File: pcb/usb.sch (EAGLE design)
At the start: 25 parts, among them J1 JSTPH, Q1 ZXMP6A13FTA, Q2 mmbt2222, Q3 mmbt2222, U1 MIC5225-3.3v, U2 CH340C, U3 MCP73831T-2ACI/OT

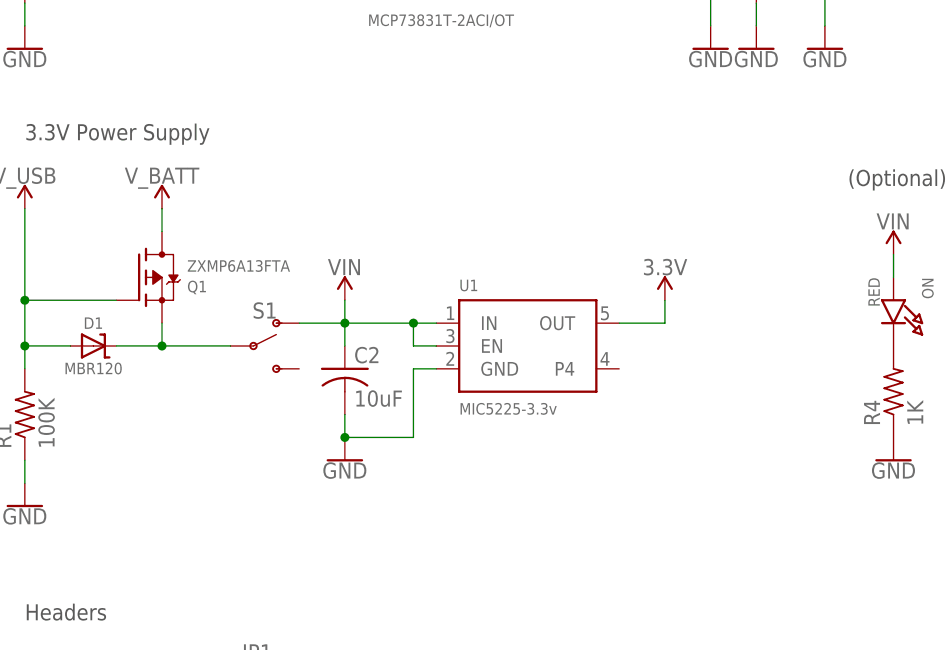
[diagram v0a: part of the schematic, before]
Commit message: Add jumper to bypass switch on USB board
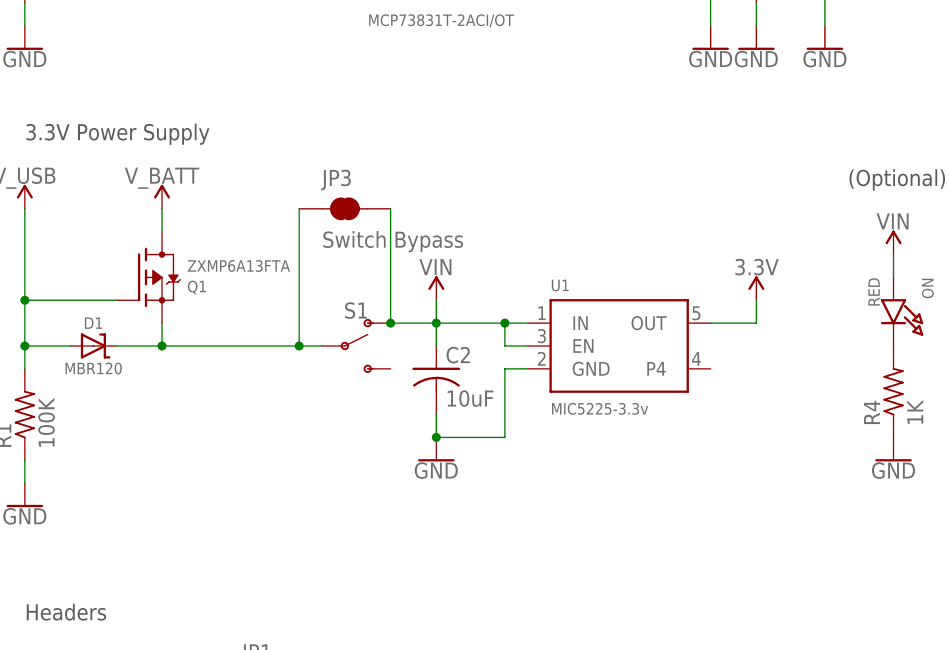
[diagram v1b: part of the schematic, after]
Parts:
- added JP3: Switch Bypass, SparkFun-Jumpers:JUMPER-SMT_2_NC_TRACE_NO-SILK
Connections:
- net N$7: now also JP3.1
- net VIN: now also JP3.2
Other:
- moved on the sheet: C2, S1, U1
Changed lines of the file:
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@@
 <attribute name="MPN" value="LMK212BJ106KG-T"/>
 </part>
+<part name="JP3" library="SparkFun-Jumpers" library_urn="urn:adsk.eagle:library:528" deviceset="JUMPER-SMT_2_NC_TRACE" device="_NO-SILK" package3d_urn="urn:adsk.eagle:package:39286/1" value="Switch Bypass"/>
 </parts>
 <sheets>
@@
 </plain>
 <instances>
-<instance part="U1" gate="G$1" x="73.66" y="68.58" smashed="yes">
-<attribute name="NAME" x="66.04" y="74.676" size="1.27" layer="95"/>
-<attribute name="VALUE" x="66.04" y="60.96" size="1.27" layer="95"/>
-<attribute name="MPN" x="73.66" y="68.58" size="1.778" layer="96" display="off"/>
+<instance part="U1" gate="G$1" x="83.82" y="68.58" smashed="yes">
+<attribute name="NAME" x="76.2" y="74.676" size="1.27" layer="95"/>
+<attribute name="VALUE" x="76.2" y="60.96" size="1.27" layer="95"/>
+<attribute name="MPN" x="83.82" y="68.58" size="1.778" layer="96" display="off"/>
 </instance>
 <instance part="U3" gate="G$1" x="66.04" y="116.84" smashed="yes">
@@
 <attribute name="MPN" x="33.02" y="76.2" size="1.778" layer="96" rot="MR180" display="off"/>
 </instance>
-<instance part="S1" gate="1" x="43.18" y="68.58" smashed="yes">
-<attribute name="NAME" x="44.45" y="71.628" size="1.778" layer="95" font="vector" align="bottom-center"/>
-<attribute name="VALUE" x="44.196" y="65.278" size="1.778" layer="96" font="vector" align="top-center"/>
-<attribute name="MPN" x="43.18" y="68.58" size="1.778" layer="96" display="off"/>
+<instance part="S1" gate="1" x="53.34" y="68.58" smashed="yes">
+<attribute name="NAME" x="54.61" y="71.628" size="1.778" layer="95" font="vector" align="bottom-center"/>
+<attribute name="VALUE" x="54.356" y="65.278" size="1.778" layer="96" font="vector" align="top-center"/>
+<attribute name="MPN" x="53.34" y="68.58" size="1.778" layer="96" display="off"/>
 </instance>
 <instance part="U2" gate="U1" x="187.96" y="119.38" smashed="yes">
@@
 <attribute name="VALUE" x="17.78" y="129.794" size="1.778" layer="96" align="bottom-center"/>
 </instance>
-<instance part="SUPPLY5" gate="G$1" x="88.9" y="73.66" smashed="yes">
-<attribute name="VALUE" x="88.9" y="76.454" size="1.778" layer="96" font="vector" align="bottom-center"/>
-</instance>
-<instance part="SUPPLY4" gate="G$1" x="53.34" y="73.66" smashed="yes">
-<attribute name="VALUE" x="53.34" y="76.454" size="1.778" layer="96" align="bottom-center"/>
+<instance part="SUPPLY5" gate="G$1" x="99.06" y="73.66" smashed="yes">
+<attribute name="VALUE" x="99.06" y="76.454" size="1.778" layer="96" font="vector" align="bottom-center"/>
+</instance>
+<instance part="SUPPLY4" gate="G$1" x="63.5" y="73.66" smashed="yes">
+<attribute name="VALUE" x="63.5" y="76.454" size="1.778" layer="96" align="bottom-center"/>
 </instance>
 <instance part="SUPPLY7" gate="G$1" x="114.3" y="78.74" smashed="yes">
@@
 <attribute name="VALUE" x="17.78" y="50.546" size="1.778" layer="96" align="top-center"/>
 </instance>
-<instance part="GND3" gate="1" x="53.34" y="55.88" smashed="yes">
-<attribute name="VALUE" x="53.34" y="55.626" size="1.778" layer="96" align="top-center"/>
+<instance part="GND3" gate="1" x="63.5" y="55.88" smashed="yes">
+<attribute name="VALUE" x="63.5" y="55.626" size="1.778" layer="96" align="top-center"/>
 </instance>
 <instance part="GND7" gate="1" x="114.3" y="55.88" smashed="yes">
@@
 <attribute name="VALUE" x="172.72" y="106.426" size="1.778" layer="96" align="top-center"/>
 </instance>
-<instance part="C2" gate="G$1" x="53.34" y="66.04" smashed="yes">
-<attribute name="NAME" x="54.356" y="66.675" size="1.778" layer="95"/>
-<attribute name="VALUE" x="54.356" y="61.849" size="1.778" layer="96"/>
-<attribute name="MPN" x="53.34" y="66.04" size="1.778" layer="96" display="off"/>
+<instance part="C2" gate="G$1" x="63.5" y="66.04" smashed="yes">
+<attribute name="NAME" x="64.516" y="66.675" size="1.778" layer="95"/>
+<attribute name="VALUE" x="64.516" y="61.849" size="1.778" layer="96"/>
+<attribute name="MPN" x="63.5" y="66.04" size="1.778" layer="96" display="off"/>
+</instance>
+<instance part="JP3" gate="G$1" x="53.34" y="83.82" smashed="yes">
+<attribute name="NAME" x="50.8" y="86.36" size="1.778" layer="95" font="vector"/>
+<attribute name="VALUE" x="50.8" y="81.28" size="1.778" layer="96" font="vector" align="top-left"/>
 </instance>
 </instances>
@@
 </segment>
 <segment>
-<wire x1="63.5" y1="66.04" x2="60.96" y2="66.04" width="0.1524" layer="91"/>
-<wire x1="60.96" y1="66.04" x2="60.96" y2="58.42" width="0.1524" layer="91"/>
-<wire x1="53.34" y1="60.96" x2="53.34" y2="58.42" width="0.1524" layer="91"/>
-<wire x1="53.34" y1="58.42" x2="60.96" y2="58.42" width="0.1524" layer="91"/>
+<wire x1="73.66" y1="66.04" x2="71.12" y2="66.04" width="0.1524" layer="91"/>
+<wire x1="71.12" y1="66.04" x2="71.12" y2="58.42" width="0.1524" layer="91"/>
+<wire x1="63.5" y1="60.96" x2="63.5" y2="58.42" width="0.1524" layer="91"/>
+<wire x1="63.5" y1="58.42" x2="71.12" y2="58.42" width="0.1524" layer="91"/>
 <pinref part="U1" gate="G$1" pin="GND"/>
 <pinref part="GND3" gate="1" pin="GND"/>
-<junction x="53.34" y="58.42"/>
+<junction x="63.5" y="58.42"/>
 <pinref part="C2" gate="G$1" pin="2"/>
 </segment>
@@
 <wire x1="27.94" y1="68.58" x2="33.02" y2="68.58" width="0.1524" layer="91"/>
 <pinref part="Q1" gate="G$1" pin="S"/>
-<wire x1="33.02" y1="68.58" x2="40.64" y2="68.58" width="0.1524" layer="91"/>
+<wire x1="33.02" y1="68.58" x2="48.26" y2="68.58" width="0.1524" layer="91"/>
+<wire x1="48.26" y1="68.58" x2="50.8" y2="68.58" width="0.1524" layer="91"/>
 <wire x1="33.02" y1="71.12" x2="33.02" y2="68.58" width="0.1524" layer="91"/>
 <junction x="33.02" y="68.58"/>
 <pinref part="S1" gate="1" pin="P"/>
+<pinref part="JP3" gate="G$1" pin="1"/>
+<wire x1="48.26" y1="83.82" x2="48.26" y2="68.58" width="0.1524" layer="91"/>
+<junction x="48.26" y="68.58"/>
 </segment>
 </net>
@@
 </segment>
 <segment>
-<wire x1="63.5" y1="71.12" x2="60.96" y2="71.12" width="0.1524" layer="91"/>
-<wire x1="60.96" y1="71.12" x2="53.34" y2="71.12" width="0.1524" layer="91"/>
-<wire x1="53.34" y1="71.12" x2="53.34" y2="73.66" width="0.1524" layer="91"/>
-<wire x1="63.5" y1="68.58" x2="60.96" y2="68.58" width="0.1524" layer="91"/>
-<wire x1="60.96" y1="68.58" x2="60.96" y2="71.12" width="0.1524" layer="91"/>
-<wire x1="53.34" y1="71.12" x2="53.34" y2="68.58" width="0.1524" layer="91"/>
-<junction x="60.96" y="71.12"/>
-<junction x="53.34" y="71.12"/>
+<wire x1="73.66" y1="71.12" x2="71.12" y2="71.12" width="0.1524" layer="91"/>
+<wire x1="71.12" y1="71.12" x2="63.5" y2="71.12" width="0.1524" layer="91"/>
+<wire x1="63.5" y1="71.12" x2="63.5" y2="73.66" width="0.1524" layer="91"/>
+<wire x1="73.66" y1="68.58" x2="71.12" y2="68.58" width="0.1524" layer="91"/>
+<wire x1="71.12" y1="68.58" x2="71.12" y2="71.12" width="0.1524" layer="91"/>
+<wire x1="63.5" y1="71.12" x2="63.5" y2="68.58" width="0.1524" layer="91"/>
+<junction x="71.12" y="71.12"/>
+<junction x="63.5" y="71.12"/>
 <pinref part="U1" gate="G$1" pin="IN"/>
 <pinref part="U1" gate="G$1" pin="EN"/>
 <pinref part="S1" gate="1" pin="O"/>
-<wire x1="48.26" y1="71.12" x2="53.34" y2="71.12" width="0.1524" layer="91"/>
+<wire x1="58.42" y1="71.12" x2="63.5" y2="71.12" width="0.1524" layer="91"/>
 <pinref part="SUPPLY4" gate="G$1" pin="VIN"/>
 <pinref part="C2" gate="G$1" pin="1"/>
+<pinref part="JP3" gate="G$1" pin="2"/>
+<wire x1="58.42" y1="83.82" x2="58.42" y2="71.12" width="0.1524" layer="91"/>
+<junction x="58.42" y="71.12"/>
 </segment>
 <segment>
@@
 </segment>
 <segment>
-<wire x1="88.9" y1="71.12" x2="88.9" y2="73.66" width="0.1524" layer="91"/>
-<wire x1="83.82" y1="71.12" x2="88.9" y2="71.12" width="0.1524" layer="91"/>
+<wire x1="99.06" y1="71.12" x2="99.06" y2="73.66" width="0.1524" layer="91"/>
+<wire x1="93.98" y1="71.12" x2="99.06" y2="71.12" width="0.1524" layer="91"/>
 <pinref part="U1" gate="G$1" pin="OUT"/>
 <pinref part="SUPPLY5" gate="G$1" pin="3.3V"/>

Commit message: Make the slots for the usb connector wider
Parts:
- J2: device Wurth_Elektronik_Electromechanic_Input-Output_Connectors_rev19b:614105150621 -> Wurth_Elektronik_Electromechanic_Input-Output_Connectors_rev19b_wider_slots:614105150621
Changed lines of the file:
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@@
 <attribute name="MPN" value="8Fx1L-254mm"/>
 </part>
-<part name="J2" library="Wurth_Elektronik_Electromechanic_Input-Output_Connectors_rev19b" library_urn="urn:adsk.eagle:library:488835" deviceset="614105150621" device="" package3d_urn="urn:adsk.eagle:package:3360156/4">
+<part name="J2" library="Wurth_Elektronik_Electromechanic_Input-Output_Connectors_rev19b_wider_slots" deviceset="614105150621" device="" package3d_urn="urn:adsk.eagle:package:3360156/4">
 <attribute name="MPN" value="614105150621"/>
 </part>

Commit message: Remove switch bypass jumper (revert c81c233)
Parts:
- removed JP3: Switch Bypass, SparkFun-Jumpers:JUMPER-SMT_2_NC_TRACE_NO-SILK
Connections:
- net N$7: no longer JP3.1
- net VIN: no longer JP3.2
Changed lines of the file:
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@@
 <attribute name="MPN" value="LMK212BJ106KG-T"/>
 </part>
-<part name="JP3" library="SparkFun-Jumpers" library_urn="urn:adsk.eagle:library:528" deviceset="JUMPER-SMT_2_NC_TRACE" device="_NO-SILK" package3d_urn="urn:adsk.eagle:package:39286/1" value="Switch Bypass"/>
 </parts>
 <sheets>
@@
 <attribute name="MPN" x="63.5" y="66.04" size="1.778" layer="96" display="off"/>
 </instance>
-<instance part="JP3" gate="G$1" x="53.34" y="83.82" smashed="yes">
-<attribute name="NAME" x="50.8" y="86.36" size="1.778" layer="95" font="vector"/>
-<attribute name="VALUE" x="50.8" y="81.28" size="1.778" layer="96" font="vector" align="top-left"/>
-</instance>
 </instances>
 <busses>
@@
 <wire x1="27.94" y1="68.58" x2="33.02" y2="68.58" width="0.1524" layer="91"/>
 <pinref part="Q1" gate="G$1" pin="S"/>
-<wire x1="33.02" y1="68.58" x2="48.26" y2="68.58" width="0.1524" layer="91"/>
-<wire x1="48.26" y1="68.58" x2="50.8" y2="68.58" width="0.1524" layer="91"/>
+<wire x1="33.02" y1="68.58" x2="50.8" y2="68.58" width="0.1524" layer="91"/>
 <wire x1="33.02" y1="71.12" x2="33.02" y2="68.58" width="0.1524" layer="91"/>
 <junction x="33.02" y="68.58"/>
 <pinref part="S1" gate="1" pin="P"/>
-<pinref part="JP3" gate="G$1" pin="1"/>
-<wire x1="48.26" y1="83.82" x2="48.26" y2="68.58" width="0.1524" layer="91"/>
-<junction x="48.26" y="68.58"/>
 </segment>
 </net>
@@
 <pinref part="SUPPLY4" gate="G$1" pin="VIN"/>
 <pinref part="C2" gate="G$1" pin="1"/>
-<pinref part="JP3" gate="G$1" pin="2"/>
-<wire x1="58.42" y1="83.82" x2="58.42" y2="71.12" width="0.1524" layer="91"/>
-<junction x="58.42" y="71.12"/>
-</segment>
-<segment>
+</segment>
+<segment>

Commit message: Add a jst-sh battery connector
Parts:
- added X1: SM02B-SRSS-TB, con-jst2.rpt:SM02B-SRSS-TB
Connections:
- net GND: now also X1-2.S
- net V_BATT: now also X1-1.S
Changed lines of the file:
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@@
 <attribute name="MPN" value="LMK212BJ106KG-T"/>
 </part>
+<part name="X1" library="con-jst2.rpt" deviceset="?M02B-SRSS-TB" device="S"/>
+<part name="SUPPLY9" library="SparkFun-PowerSymbols" library_urn="urn:adsk.eagle:library:530" deviceset="V_BATT" device=""/>
+<part name="GND12" library="SparkFun-PowerSymbols" library_urn="urn:adsk.eagle:library:530" deviceset="GND" device=""/>
 </parts>
 <sheets>
@@
 <attribute name="MPN" x="63.5" y="66.04" size="1.778" layer="96" display="off"/>
 </instance>
+<instance part="X1" gate="-1" x="129.54" y="121.92" smashed="yes">
+<attribute name="NAME" x="132.08" y="121.158" size="1.524" layer="95"/>
+<attribute name="VALUE" x="128.778" y="123.317" size="1.524" layer="96"/>
+</instance>
+<instance part="X1" gate="-2" x="129.54" y="119.38" smashed="yes">
+<attribute name="NAME" x="132.08" y="118.618" size="1.524" layer="95"/>
+</instance>
+<instance part="SUPPLY9" gate="G$1" x="124.46" y="129.54" smashed="yes">
+<attribute name="VALUE" x="124.46" y="132.334" size="1.778" layer="96" align="bottom-center"/>
+</instance>
+<instance part="GND12" gate="1" x="124.46" y="109.22" smashed="yes">
+<attribute name="VALUE" x="124.46" y="108.966" size="1.778" layer="96" align="top-center"/>
+</instance>
 </instances>
 <busses>
@@
 <wire x1="172.72" y1="109.22" x2="177.8" y2="109.22" width="0.1524" layer="91"/>
 <pinref part="GND11" gate="1" pin="GND"/>
+</segment>
+<segment>
+<pinref part="X1" gate="-2" pin="S"/>
+<wire x1="127" y1="119.38" x2="124.46" y2="119.38" width="0.1524" layer="91"/>
+<pinref part="GND12" gate="1" pin="GND"/>
+<wire x1="124.46" y1="119.38" x2="124.46" y2="111.76" width="0.1524" layer="91"/>
 </segment>
 </net>
@@
 <pinref part="SUPPLY6" gate="G$1" pin="V_BATT"/>
 </segment>
-</net>
+<segment>
+<pinref part="SUPPLY9" gate="G$1" pin="V_BATT"/>
+<wire x1="124.46" y1="129.54" x2="124.46" y2="121.92" width="0.1524" layer="91"/>
+<pinref part="X1" gate="-1" pin="S"/>
+<wire x1="124.46" y1="121.92" x2="127" y2="121.92" width="0.1524" layer="91"/>
+</segment>
+</net>
